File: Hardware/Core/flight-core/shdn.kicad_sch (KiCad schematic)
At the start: 24 parts, among them J27 TILT, J29 Conn_01x02, J30 Conn_01x02, J3101 Conn_02x02_Remote_ESTOP, J3103 Conn_02x07_Counter_Clockwise, J3301 Conn_02x02_Remote_ESTOP, J3302 Conn_02x02_Remote_ESTOP, J3303 Conn_02x02_Remote_ESTOP, J3304 Conn_02x02_Remote_ESTOP, J3305 Conn_02x02_Remote_ESTOP, J3306 Conn_02x02_Remote_ESTOP, J3307 Conn_02x02_Remote_ESTOP, J3309 Conn_02x02_Remote_ESTOP, Q16 MMBF170, U3101 LTV-356T, U65 LTV-356T

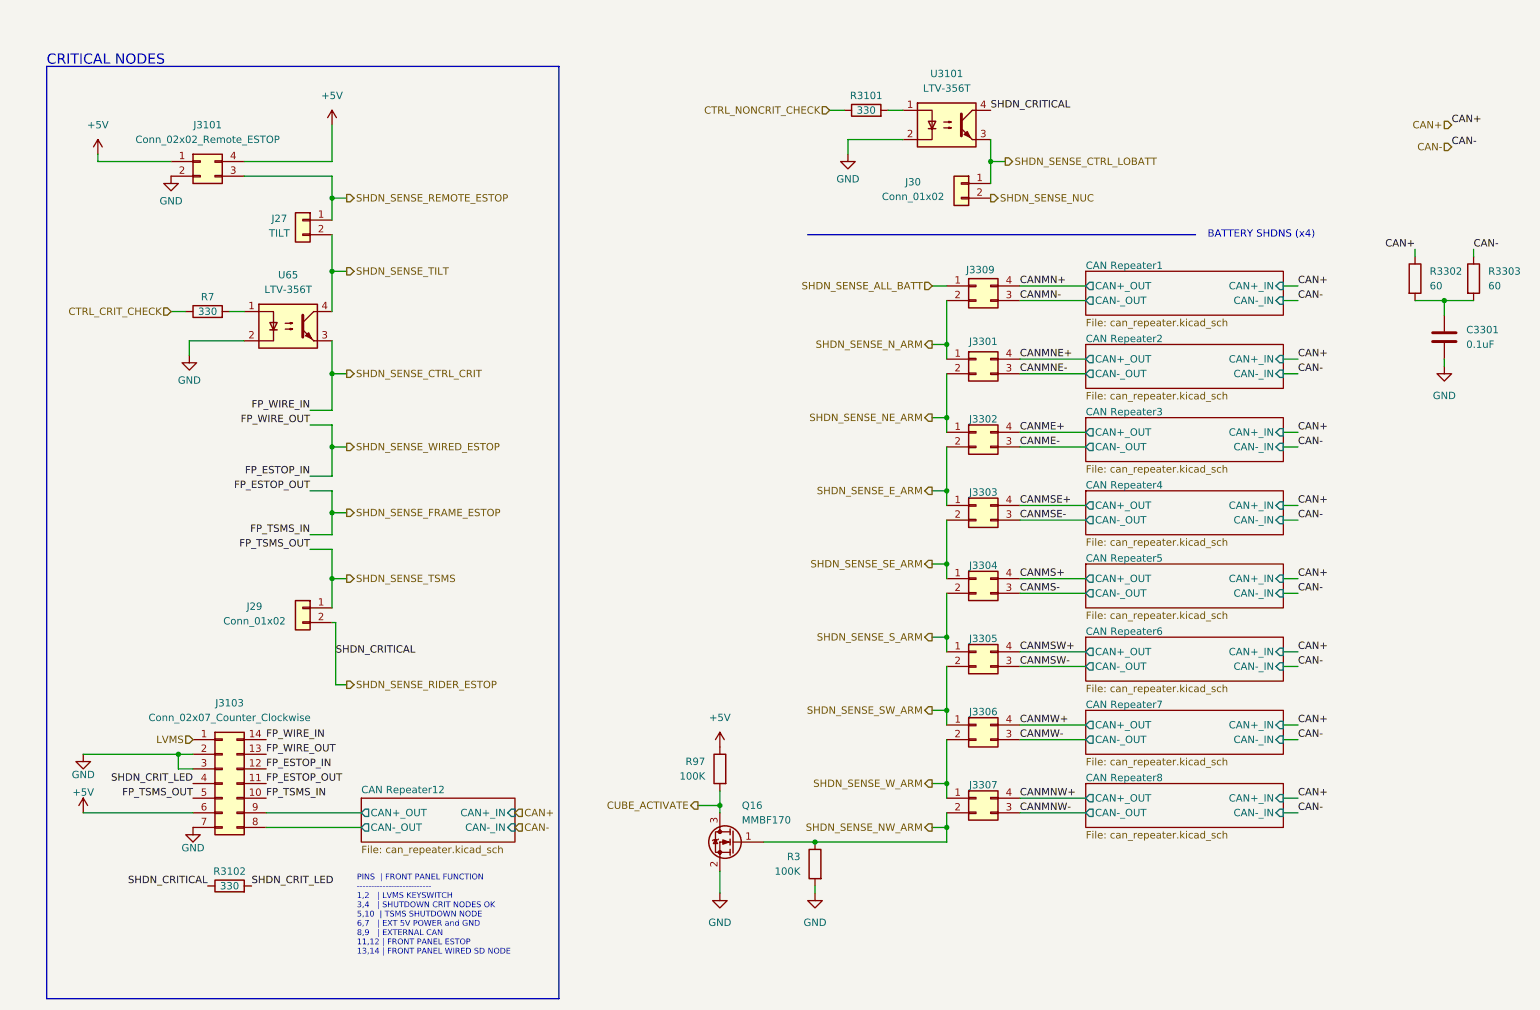
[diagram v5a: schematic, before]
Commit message: minor erc fixes (grid, reannotation, updated footprint associations)
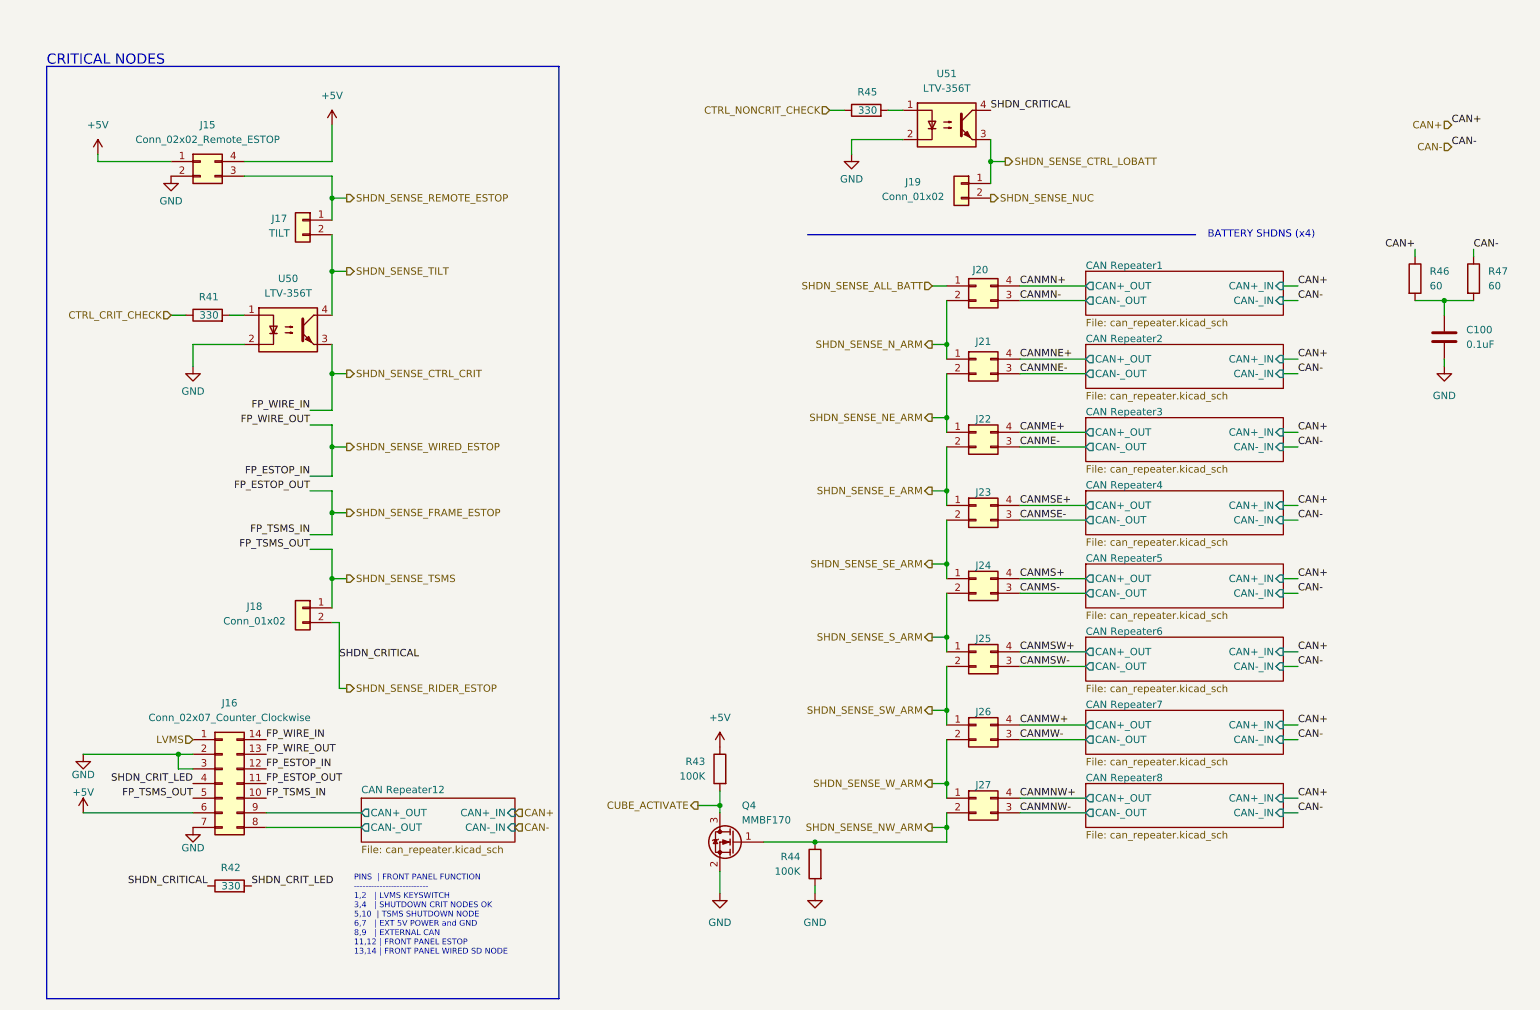
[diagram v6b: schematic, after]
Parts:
- removed R3101, R3102, R7: 330, OEM:R_0603_1608Metric, symbol OEM:1KR
- added R41, R42, R45: 330, footprints:R_0603_1608Metric, symbol Device:R
- J16: renamed from J3103; footprint (none) -> obad_footprints:MicroFit_VT_2x7
- J17: renamed from J27; footprint (none) -> footprints:MicroFit_V_2
- J18: renamed from J29; footprint (none) -> footprints:MicroFit_V_2
- J19: renamed from J30; footprint (none) -> footprints:MicroFit_V_2
- Q4: renamed from Q16; footprint TO_SOT_Packages_SMD:SOT-23 -> Package_TO_SOT_SMD:SOT-23
- renumbered C3301 to C100, J3101 to J15, J3309 to J20, J3301 to J21, J3302 to J22, J3303 to J23, J3304 to J24, J3305 to J25, J3306 to J26, J3307 to J27, R97 to R43, R3 to R44, R3302 to R46, R3303 to R47, U65 to U50, U3101 to U51
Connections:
- net CTRL_CRIT_CHECK: now also R41.1
- net CTRL_NONCRIT_CHECK: now also R45.1
- net SHDN_CRIT_LED: now also R42.2
- net SHDN_SENSE_RIDER_ESTOP: now also R42.1
- net at U50.1: now also R41.2
- net at U51.1: now also R45.2
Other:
- moved on the sheet: U50

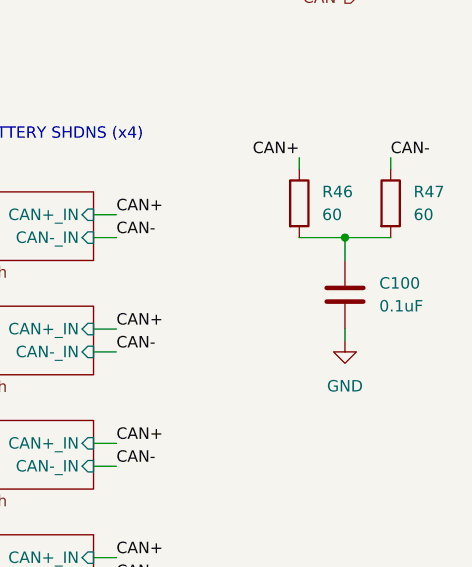
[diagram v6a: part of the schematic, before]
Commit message: added sense pwr cycle pull down, low side cube mosfets, fixed mosi/miso swap on i/o expander, Rs -> generic, reannotated
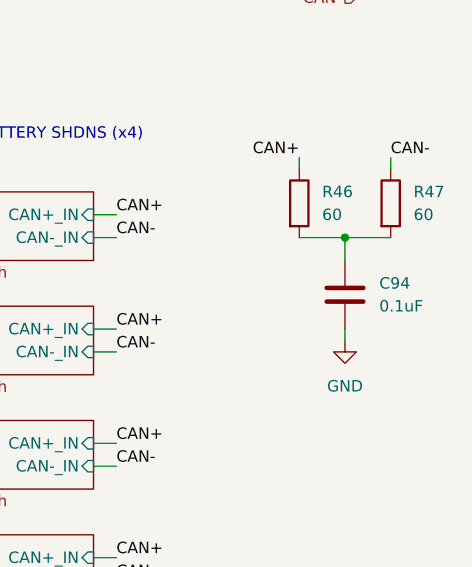
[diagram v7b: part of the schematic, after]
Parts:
- renumbered C100 to C94
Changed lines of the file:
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@@
 		(dnp no)
 		(fields_autoplaced yes)
-		(property "Reference" "#PWR0198"
+		(property "Reference" "#PWR0199"
 			(at 138.43 173.99 0)
 			(effects
@@
 			(project "flight-core"
 				(path "/93f46f4b-cdf5-47ec-af03-96378e73b2e1/04eec032-1078-43ee-b9a1-985f3959b29a"
-					(reference "#PWR0198")
+					(reference "#PWR0199")
 					(unit 1)
 				)
@@
 		(dnp no)
 		(fields_autoplaced yes)
-		(property "Reference" "#PWR0199"
+		(property "Reference" "#PWR0200"
 			(at 154.94 173.99 0)
 			(effects
@@
 			(project "flight-core"
 				(path "/93f46f4b-cdf5-47ec-af03-96378e73b2e1/04eec032-1078-43ee-b9a1-985f3959b29a"
-					(reference "#PWR0199")
+					(reference "#PWR0200")
 					(unit 1)
 				)
@@
 		(on_board yes)
 		(dnp no)
-		(property "Reference" "#PWR0191"
+		(property "Reference" "#PWR0192"
 			(at 27.94 157.48 0)
 			(effects
@@
 			(project "flight-core"
 				(path "/93f46f4b-cdf5-47ec-af03-96378e73b2e1/04eec032-1078-43ee-b9a1-985f3959b29a"
-					(reference "#PWR0191")
+					(reference "#PWR0192")
 					(unit 1)
 				)
@@
 		(dnp no)
 		(fields_autoplaced yes)
-		(property "Reference" "#PWR0201"
+		(property "Reference" "#PWR0202"
 			(at 264.16 82.55 0)
 			(effects
@@
 			(project "flight-core"
 				(path "/93f46f4b-cdf5-47ec-af03-96378e73b2e1/04eec032-1078-43ee-b9a1-985f3959b29a"
-					(reference "#PWR0201")
+					(reference "#PWR0202")
 					(unit 1)
 				)
@@
 		(dnp no)
 		(fields_autoplaced yes)
-		(property "Reference" "C100"
+		(property "Reference" "C94"
 			(at 267.97 69.8499 0)
 			(effects
@@
 			(project "flight-core"
 				(path "/93f46f4b-cdf5-47ec-af03-96378e73b2e1/04eec032-1078-43ee-b9a1-985f3959b29a"
-					(reference "C100")
+					(reference "C94")
 					(unit 1)
 				)
@@
 		(on_board yes)
 		(dnp no)
-		(property "Reference" "#PWR0190"
+		(property "Reference" "#PWR0191"
 			(at 27.94 149.86 0)
 			(effects
@@
 			(project "flight-core"
 				(path "/93f46f4b-cdf5-47ec-af03-96378e73b2e1/04eec032-1078-43ee-b9a1-985f3959b29a"
-					(reference "#PWR0190")
+					(reference "#PWR0191")
 					(unit 1)
 				)
@@
 		(dnp no)
 		(fields_autoplaced yes)
-		(property "Reference" "#PWR0196"
+		(property "Reference" "#PWR0197"
 			(at 71.12 38.1 0)
 			(effects
@@
 			(project "flight-core"
 				(path "/93f46f4b-cdf5-47ec-af03-96378e73b2e1/04eec032-1078-43ee-b9a1-985f3959b29a"
-					(reference "#PWR0196")
+					(reference "#PWR0197")
 					(unit 1)
 				)
@@
 		(on_board yes)
 		(dnp no)
-		(property "Reference" "#PWR0200"
+		(property "Reference" "#PWR0201"
 			(at 161.29 45.72 0)
 			(effects
@@
 			(project "flight-core"
 				(path "/93f46f4b-cdf5-47ec-af03-96378e73b2e1/04eec032-1078-43ee-b9a1-985f3959b29a"
-					(reference "#PWR0200")
+					(reference "#PWR0201")
 					(unit 1)
 				)
@@
 		(on_board yes)
 		(dnp no)
-		(property "Reference" "#PWR0193"
+		(property "Reference" "#PWR0194"
 			(at 43.18 49.53 0)
 			(effects
@@
 			(project "flight-core"
 				(path "/93f46f4b-cdf5-47ec-af03-96378e73b2e1/04eec032-1078-43ee-b9a1-985f3959b29a"
-					(reference "#PWR0193")
+					(reference "#PWR0194")
 					(unit 1)
 				)
@@
 		(dnp no)
 		(fields_autoplaced yes)
-		(property "Reference" "#PWR0192"
+		(property "Reference" "#PWR0193"
 			(at 30.48 43.18 0)
 			(effects
@@
 			(project "flight-core"
 				(path "/93f46f4b-cdf5-47ec-af03-96378e73b2e1/04eec032-1078-43ee-b9a1-985f3959b29a"
-					(reference "#PWR0192")
+					(reference "#PWR0193")
 					(unit 1)
 				)
@@
 		(on_board yes)
 		(dnp no)
-		(property "Reference" "#PWR0195"
+		(property "Reference" "#PWR0196"
 			(at 46.99 162.56 0)
 			(effects
@@
 			(project "flight-core"
 				(path "/93f46f4b-cdf5-47ec-af03-96378e73b2e1/04eec032-1078-43ee-b9a1-985f3959b29a"
-					(reference "#PWR0195")
+					(reference "#PWR0196")
 					(unit 1)
 				)
@@
 		(on_board yes)
 		(dnp no)
-		(property "Reference" "#PWR0194"
+		(property "Reference" "#PWR0195"
 			(at 46.99 82.55 0)
 			(effects
@@
 			(project "flight-core"
 				(path "/93f46f4b-cdf5-47ec-af03-96378e73b2e1/04eec032-1078-43ee-b9a1-985f3959b29a"
-					(reference "#PWR0194")
+					(reference "#PWR0195")
 					(unit 1)
 				)
@@
 		(dnp no)
 		(fields_autoplaced yes)
-		(property "Reference" "#PWR0197"
+		(property "Reference" "#PWR0198"
 			(at 138.43 146.05 0)
 			(effects
@@
 			(project ""
 				(path "/93f46f4b-cdf5-47ec-af03-96378e73b2e1/04eec032-1078-43ee-b9a1-985f3959b29a"
-					(reference "#PWR0197")
-					(unit 1)
-				)
+					(reference "#PWR0198")
+					(unit 1)
+				)

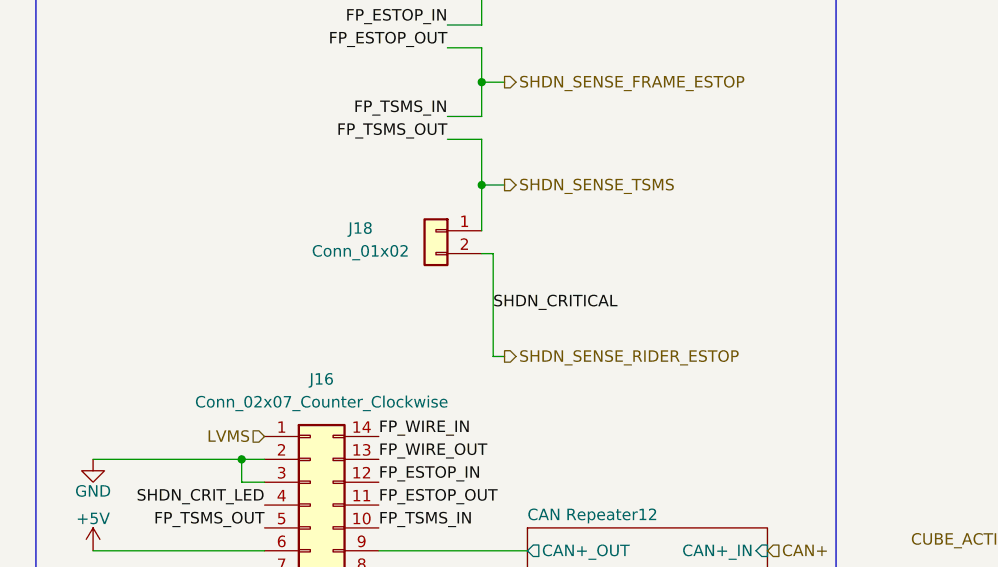
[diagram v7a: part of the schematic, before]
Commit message: replicated layout for all can repeaters, placed in shutdown order; added rider lower estop in schem; j18 is 4 pin
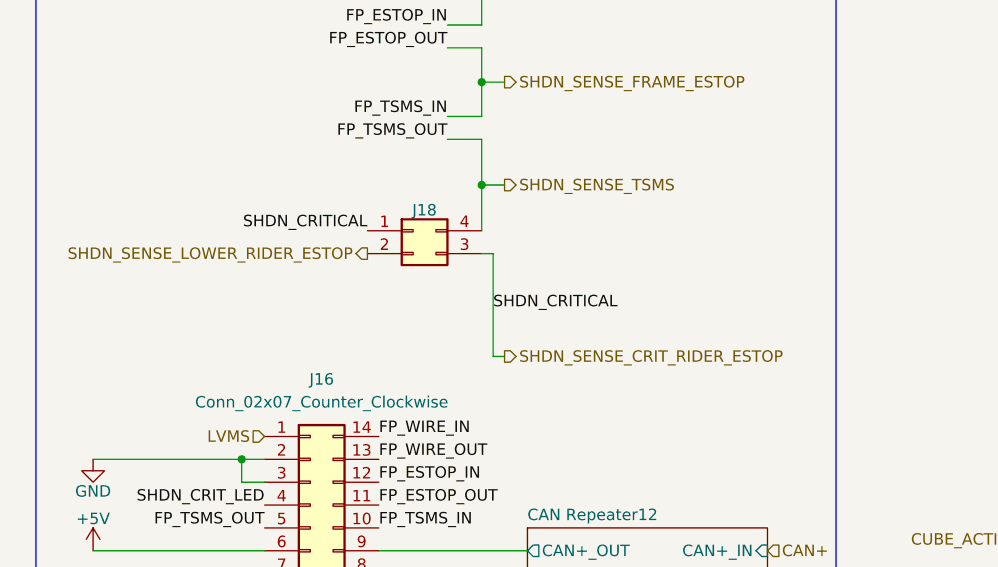
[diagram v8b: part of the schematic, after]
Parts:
- removed J18: Conn_01x02, footprints:MicroFit_V_2, symbol Connector_Generic:Conn_01x02
- added J18: Conn_02x02_Remote_ESTOP, Connector_Molex:Molex_Micro-Fit_3.0_43045-0400_2x02_P3.00mm_Horizontal, symbol Connector_Generic:Conn_02x02_Counter_Clockwise
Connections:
- net SHDN_SENSE_TSMS: now also J18.4 (Pin_4)
- net SHDN_SENSE_RIDER_ESTOP renamed SHDN_SENSE_CRIT_RIDER_ESTOP
- net SHDN_SENSE_CRIT_RIDER_ESTOP: now also J18.1 (Pin_1), J18.3 (Pin_3)
- new net SHDN_SENSE_LOWER_RIDER_ESTOP: J18.2 (Pin_2)
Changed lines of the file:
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@@
+		)
+	)
+	(label "SHDN_CRITICAL"
+		(at 58.42 118.11 180)
+		(effects
+			(font
+				(size 1.27 1.27)
+			)
+			(justify right bottom)
 		)
 	)
@@
 		)
 	)
-	(hierarchical_label "SHDN_SENSE_RIDER_ESTOP"
+	(hierarchical_label "SHDN_SENSE_CRIT_RIDER_ESTOP"
 		(shape output)
 		(at 73.66 132.08 0)
@@
 		(shape output)
 		(at 175.26 148.59 180)
+		(effects
+			(font
+				(size 1.27 1.27)
+			)
+			(justify right)
+		)
+	)
+	(hierarchical_label "SHDN_SENSE_LOWER_RIDER_ESTOP"
+		(shape output)
+		(at 58.42 120.65 180)
 		(effects
 			(font
@@
 	)
 	(symbol
-		(lib_id "Connector_Generic:Conn_01x02")
-		(at 66.04 118.11 0)
-		(mirror y)
-		(unit 1)
-		(exclude_from_sim no)
-		(in_bom yes)
-		(on_board yes)
-		(dnp no)
-		(property "Reference" "J18"
-			(at 57.658 117.856 0)
-			(effects
-				(font
-					(size 1.27 1.27)
-				)
-			)
-		)
-		(property "Value" "Conn_01x02"
-			(at 57.658 120.396 0)
-			(effects
-				(font
-					(size 1.27 1.27)
-				)
-			)
-		)
-		(property "Footprint" "footprints:MicroFit_V_2"
-			(at 66.04 118.11 0)
-			(effects
-				(font
-					(size 1.27 1.27)
-				)
-				(hide yes)
-			)
-		)
-		(property "Datasheet" "~"
-			(at 66.04 118.11 0)
-			(effects
-				(font
-					(size 1.27 1.27)
-				)
-				(hide yes)
-			)
-		)
-		(property "Description" "Generic connector, single row, 01x02, script generated (kicad-library-utils/schlib/autogen/connector/)"
-			(at 66.04 118.11 0)
-			(effects
-				(font
-					(size 1.27 1.27)
-				)
-				(hide yes)
-			)
-		)
-		(pin "1"
-		)
-		(pin "2"
-		)
-		(instances
-			(project "flight-core"
-				(path "/93f46f4b-cdf5-47ec-af03-96378e73b2e1/04eec032-1078-43ee-b9a1-985f3959b29a"
-					(reference "J18")
-					(unit 1)
-				)
-			)
-		)
-	)
-	(symbol
 		(lib_id "Isolator:LTV-356T")
 		(at 63.5 69.85 0)
@@
 					(unit 1)
 				)
+			)
+		)
+	)
+	(symbol
+		(lib_id "Connector_Generic:Conn_02x02_Counter_Clockwise")
+		(at 63.5 118.11 0)
+		(unit 1)
+		(exclude_from_sim no)
+		(in_bom yes)
+		(on_board yes)
+		(dnp no)
+		(property "Reference" "J18"
+			(at 64.77 115.824 0)
+			(effects
+				(font
+					(size 1.27 1.27)
+				)
+			)
+		)
+		(property "Value" "Conn_02x02_Remote_ESTOP"
+			(at 64.77 114.3 0)
+			(effects
+				(font
+					(size 1.27 1.27)
+				)
+				(hide yes)
+			)
+		)
+		(property "Footprint" "Connector_Molex:Molex_Micro-Fit_3.0_43045-0400_2x02_P3.00mm_Horizontal"
+			(at 63.5 118.11 0)
+			(effects
+				(font
+					(size 1.27 1.27)
+				)
+				(hide yes)
+			)
+		)
+		(property "Datasheet" "~"
+			(at 63.5 118.11 0)
+			(effects
+				(font
+					(size 1.27 1.27)
+				)
+				(hide yes)
+			)
+		)
+		(property "Description" "Generic connector, double row, 02x02, counter clockwise pin numbering scheme (similar to DIP package numbering), script generated (kicad-library-utils/schlib/autogen/connector/)"
+			(at 63.5 118.11 0)
+			(effects
+				(font
+					(size 1.27 1.27)
+				)
+				(hide yes)
+			)
+		)
+		(pin "2"
+		)
+		(pin "4"
+		)
+		(pin "1"
+		)
+		(pin "3"
+		)
+		(instances
+			(project "flight-core"
+				(path "/93f46f4b-cdf5-47ec-af03-96378e73b2e1/04eec032-1078-43ee-b9a1-985f3959b29a"
+					(reference "J18")
+					(unit 1)
+				)
